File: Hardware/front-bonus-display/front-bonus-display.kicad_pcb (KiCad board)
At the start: 4 copper layers, 44 x 34 mm, 11 parts, among them J101 Conn_02x05_Odd_Even, U101 AT24CS32-SSHM

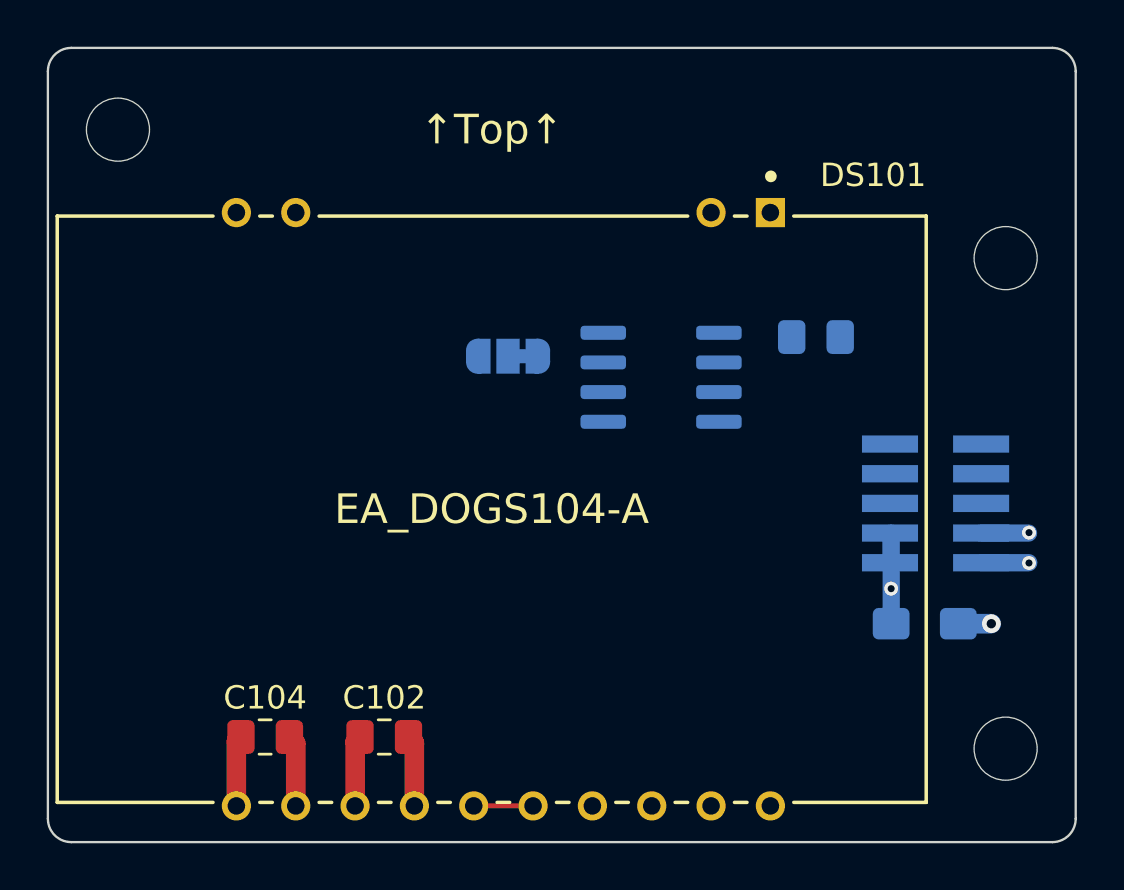
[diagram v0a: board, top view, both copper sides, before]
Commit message: Finish routing of bonus display
- Completed layout and routing of the bonus display; this is just the
  LED driver (with discrete transistors for each of the three possible
  cathode channels, and associated current limiting resistors)

- Added an improved TO-247 dual pin footprint with larger holes for the
  power resistors to be used on the analog board
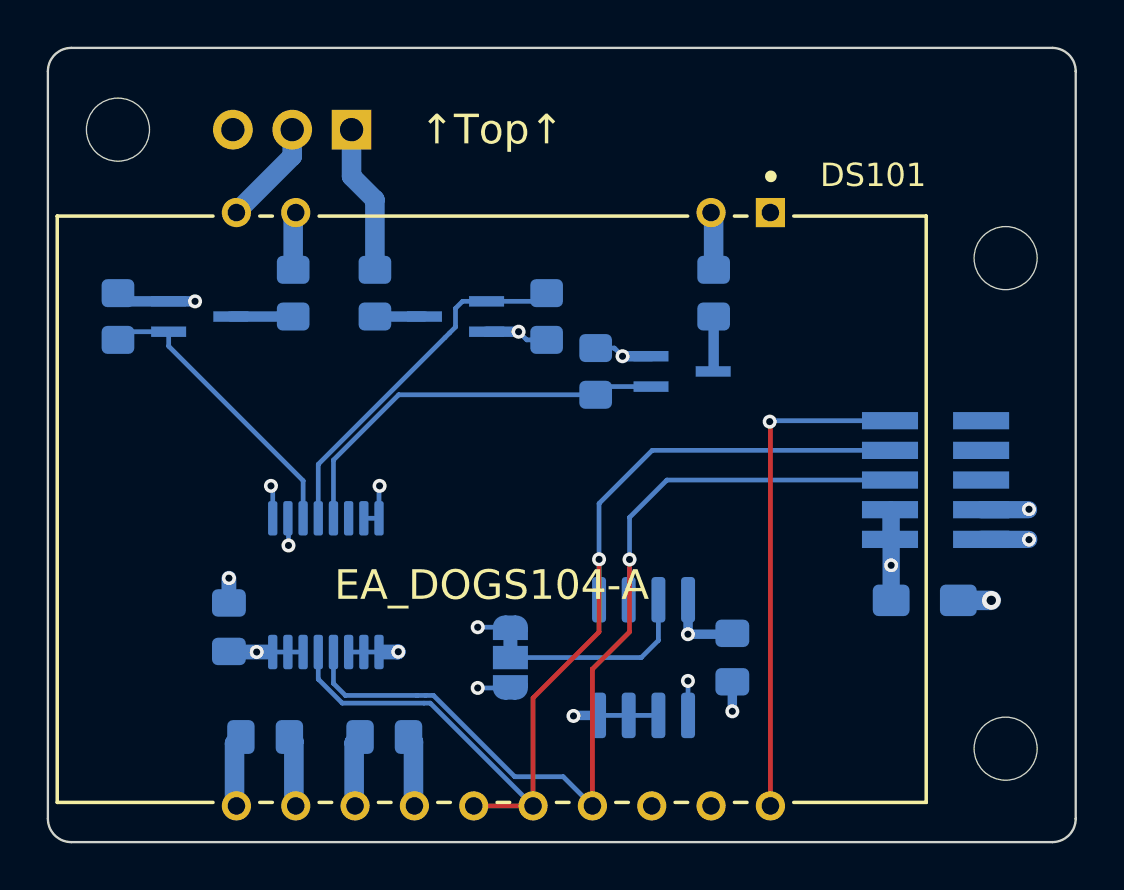
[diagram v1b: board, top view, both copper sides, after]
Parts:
- added C105: 100nF, Capacitor_SMD:C_0805_2012Metric_Pad1.18x1.45mm_HandSolder, B.Cu at (27.8, 44.8)
- added JP102: Jumper_3_Open, Connector_PinHeader_2.54mm:PinHeader_1x03_P2.54mm_Vertical, B.Cu at (33.0, 23.5)
- added Q101: MMBT3904, Package_TO_SOT_SMD:SOT-323_SC-70_Handsoldering, B.Cu at (26.5, 31.5)
- added Q102: MMBT3904, Package_TO_SOT_SMD:SOT-323_SC-70_Handsoldering, B.Cu at (37.5, 31.5)
- added Q103: MMBT3904, Package_TO_SOT_SMD:SOT-323_SC-70_Handsoldering, B.Cu at (47.1, 33.9)
- added R101: 27R, Resistor_SMD:R_0805_2012Metric_Pad1.20x1.40mm_HandSolder, B.Cu at (48.5, 30.5)
- added R102: 10R, Resistor_SMD:R_0805_2012Metric_Pad1.20x1.40mm_HandSolder, B.Cu at (34.0, 30.5)
- added R103: 20R, Resistor_SMD:R_0805_2012Metric_Pad1.20x1.40mm_HandSolder, B.Cu at (30.5, 30.5)
- added R104: 10k, Resistor_SMD:R_0805_2012Metric_Pad1.20x1.40mm_HandSolder, B.Cu at (23.0, 31.5)
- added R105: 10k, Resistor_SMD:R_0805_2012Metric_Pad1.20x1.40mm_HandSolder, B.Cu at (41.4, 31.5)
- added R106: 10k, Resistor_SMD:R_0805_2012Metric_Pad1.20x1.40mm_HandSolder, B.Cu at (43.5, 33.9)
- added U102: PCA9633, Package_SO:TSSOP-16_4.4x5mm_P0.65mm, B.Cu at (31.9, 43.0)
- C102, C104: moved to B.Cu
- moved C103 14.2 mm to (49.3, 46.1), turned to -90 degrees
- moved JP101 12.9 mm to (39.8, 46.1), turned to -90 degrees
- moved U101 12.0 mm to (45.5, 46.1), turned to 90 degrees
- moved C101 1.00 mm to (57.5, 43.6)
- moved J101 1.00 mm to (58.0, 38.5)
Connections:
- DS101 pad 1: unconnected-(DS101-Pad1) -> +3V3
- DS101 pad 10: unconnected-(DS101-Pad10) -> Net-(DS101-Pad10)
- DS101 pad 17: /I²C_SCL -> /I2C_SCL
- DS101 pad 2: unconnected-(DS101-Pad2) -> Net-(DS101-Pad2)
- DS101 pad 9: unconnected-(DS101-Pad9) -> Net-(DS101-Pad9)
- J101 pad 5: unconnected-(J101-Pad5) -> /I2C_SCL
- J101 pad 7: unconnected-(J101-Pad7) -> /I2C_SDA
- J101 pad 8: unconnected-(J101-Pad8) -> /~{IRQ}
- J101 pad 9: unconnected-(J101-Pad9) -> /~{RESET}
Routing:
- net /I2C_SDA: track 2.54 -> 45.4 mm, vias 0 -> 1
- net /I2C_SCL: track 0.00 -> 42.2 mm, vias 0 -> 1
- net /~{RESET}: track 0.00 -> 21.6 mm, vias 0 -> 1
- net GND: track 11.6 -> 32.9 mm, vias 3 -> 13
- net Net-(Q103-Pad1): track 0.00 -> 17.4 mm
- net Net-(Q102-Pad1): track 0.00 -> 15.6 mm
- net Net-(Q101-Pad1): track 0.00 -> 12.7 mm
- net +3V3: track 8.44 -> 19.2 mm, vias 1 -> 6
- net Net-(JP101-Pad2): track 0.00 -> 8.38 mm
- net Net-(JP102-Pad1): track 0.00 -> 6.41 mm
- net Net-(DS101-Pad10): track 0.00 -> 4.54 mm
- net /LED_C3: track 0.00 -> 2.67 mm
- net Net-(DS101-Pad9): track 0.00 -> 2.50 mm
- net Net-(DS101-Pad2): track 0.00 -> 2.50 mm
- net /LED_C1: track 0.00 -> 2.36 mm
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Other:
- board text added: "Load Bonus Display"
- board text added: "Rev 1"
- board text removed: "Programmable Load Bonus Display"

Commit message: Work on layout analog board
- Moved the heatsink to be horizontal near the bottom of the analog
  board, to give more open space for the analog circuitry away from the
  hot MOSFETs

- Minor tweak to bonus display (cutout for front panel jacks)
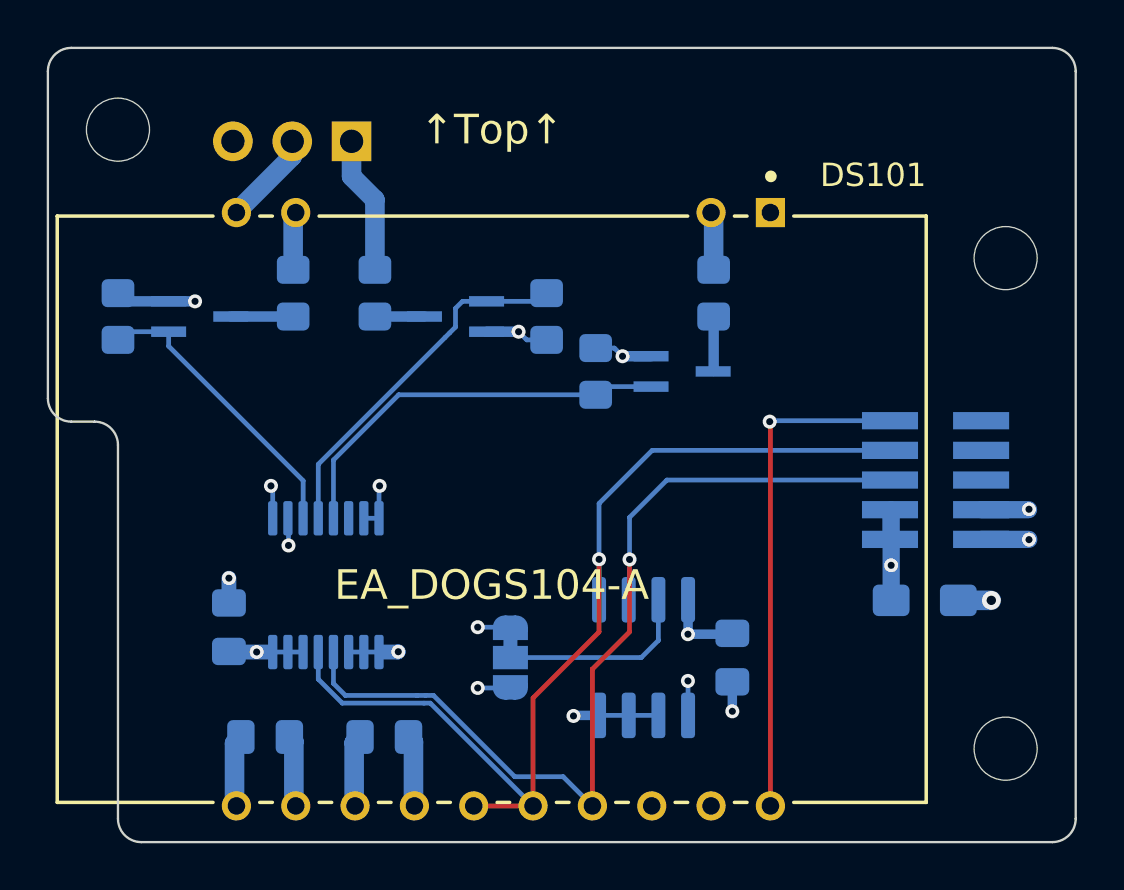
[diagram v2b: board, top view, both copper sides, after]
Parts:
- added kibuzzard-627F2330: G***, kibuzzard-627F2330, B.Cu at (33.0, 21.2)
- added kibuzzard-627F235A: G***, kibuzzard-627F235A, B.Cu at (27.9, 21.2)
- moved JP102 0.50 mm to (33.0, 24.0)
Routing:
- net Net-(JP102-Pad1): track 6.41 -> 5.91 mm
- net Net-(DS101-Pad10): track 4.54 -> 4.04 mm
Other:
- outline, holes or cut-outs redrawn
- board text added: "Cutout for input jacks"
